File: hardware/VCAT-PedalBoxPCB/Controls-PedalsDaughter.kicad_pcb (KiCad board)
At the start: 2 copper layers, 53 x 66.2 mm, 105 parts, among them IC1 AP2205-W5-7, IC2 AP2205-W5-7, J3 Conn_02x03_Top_Bottom, J4 Conn_02x06_Top_Bottom, J5 Conn_02x04_Top_Bottom, U1 TLV9002QDRQ1, U2 INA241A5xD, U3 TLV9002QDRQ1, U4 INA241A5xD, U5 TLV9002QDRQ1

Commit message: mikea
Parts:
- R11, R12, R25, R26, R35, R36: value 100 -> 120

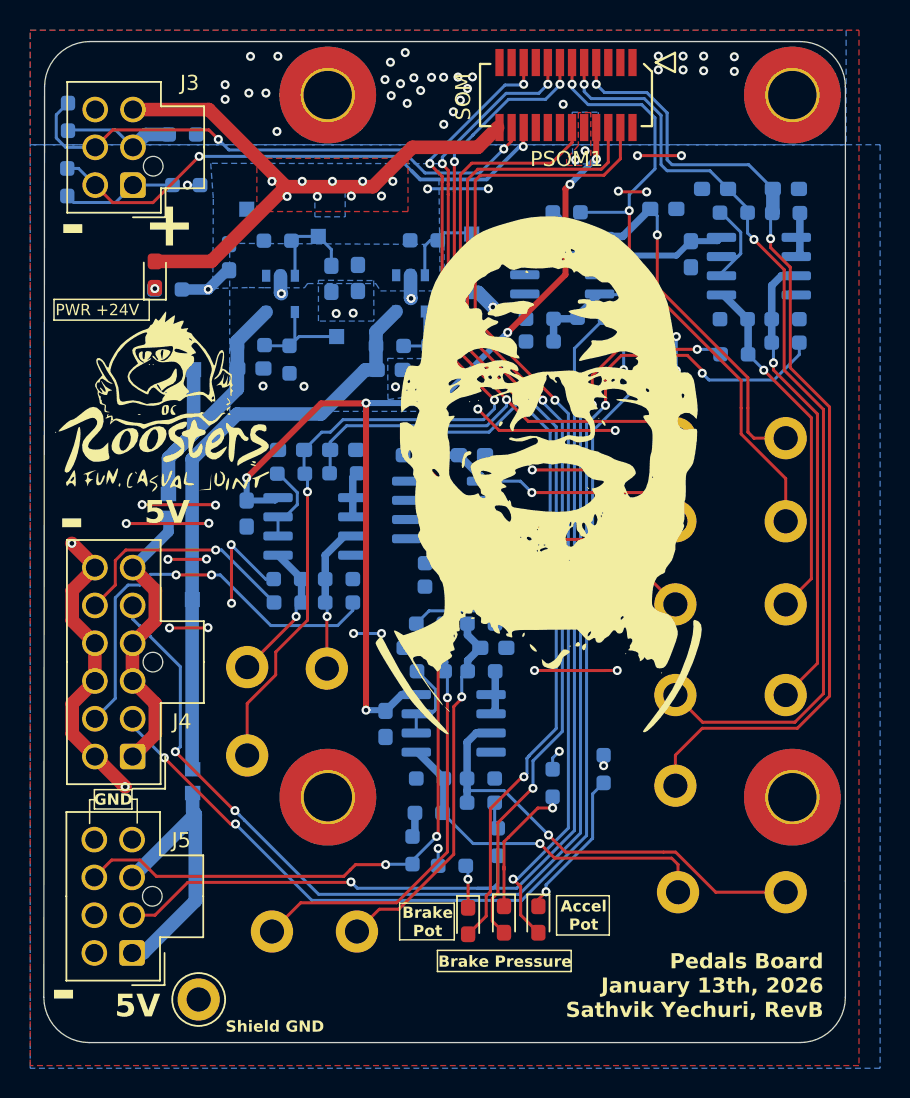
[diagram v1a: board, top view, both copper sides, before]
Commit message: layout fixes
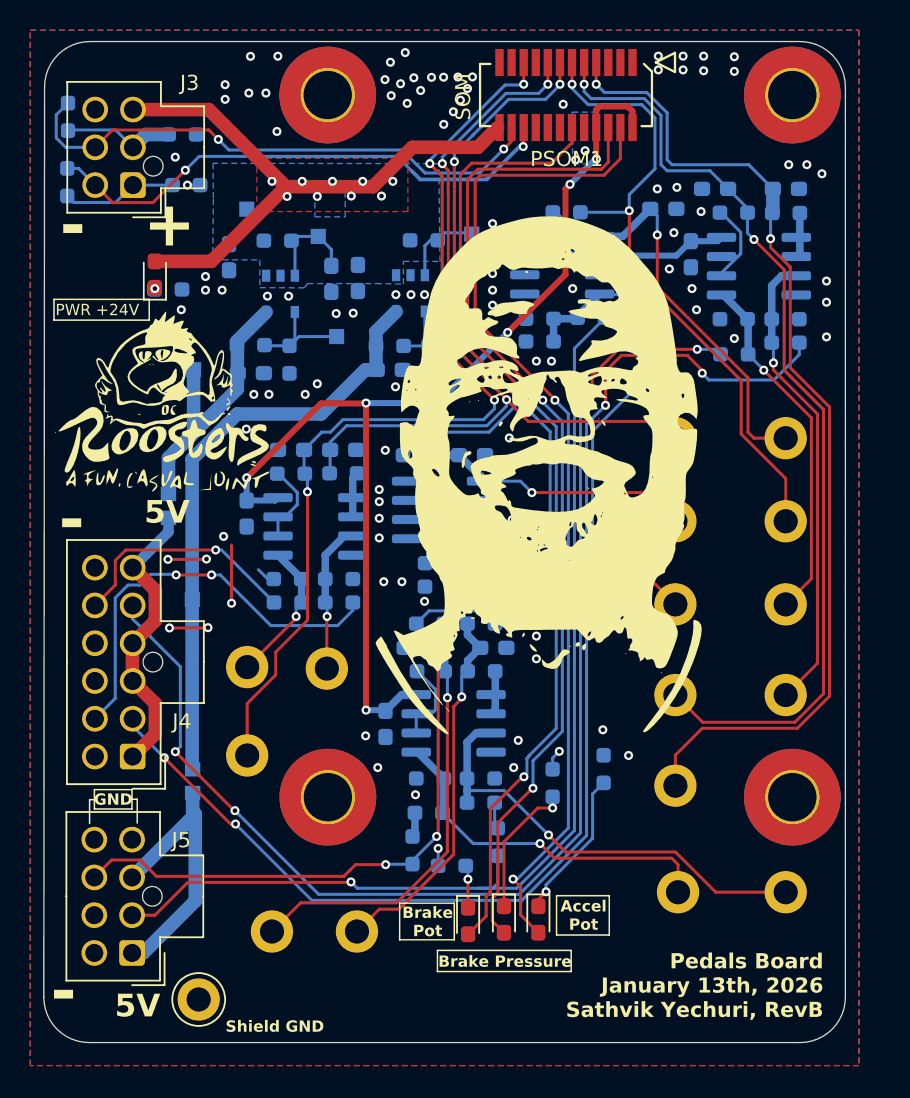
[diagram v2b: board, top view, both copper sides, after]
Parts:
- moved C7 0.32 mm to (134.6, 92.7)
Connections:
- C1 pad 1: +VDDA -> +3.3V
- C1 pad 2: GNDA -> GND
- C10 pad 2: GNDA -> GND
- C11 pad 1: GNDA -> GND
- C12 pad 1: GNDA -> GND
- C17 pad 1: +VDDA -> +3.3V
- C17 pad 2: GNDA -> GND
- C18 pad 1: GNDA -> GND
- C19 pad 1: GNDA -> GND
- C2 pad 1: GNDA -> GND
- C3 pad 1: GNDA -> GND
- C6 pad 1: +VDDA -> +3.3V
- C6 pad 2: GNDA -> GND
- C9 pad 2: GNDA -> GND
- J4 pad 10: GNDA -> GND
- J4 pad 12: GNDA -> GND
- J4 pad 7: GNDA -> GND
- J4 pad 9: GNDA -> GND
- J5 pad 5: GNDA -> GND
- J5 pad 6: GNDA -> GND
- PSOM1 pad 10: GNDA -> GND
- PSOM1 pad 2: unconnected-(PSOM1-+3.3v-Pad2) -> +3.3V
- PSOM1 pad 8: +VDDA -> +3.3V
- R1 pad 1: GNDA -> GND
- R16 pad 1: GNDA -> GND
- R23 pad 1: GNDA -> GND
- R24 pad 1: GNDA -> GND
- R30 pad 1: GNDA -> GND
- R31 pad 1: GNDA -> GND
- R32 pad 1: GNDA -> GND
- R4 pad 1: GNDA -> GND
- R40 pad 1: GNDA -> GND
- R5 pad 1: GNDA -> GND
- U1 pad 4: GNDA -> GND
- U1 pad 8: +VDDA -> +3.3V
- U2 pad 1: GNDA -> GND
- U2 pad 2: GNDA -> GND
- U2 pad 3: GNDA -> GND
- U2 pad 4: GNDA -> GND
- U2 pad 6: +VDDA -> +3.3V
- U2 pad 7: GNDA -> GND
- U3 pad 4: GNDA -> GND
- U3 pad 8: +VDDA -> +3.3V
- U4 pad 1: GNDA -> GND
- U4 pad 2: GNDA -> GND
- U4 pad 3: GNDA -> GND
- U4 pad 4: GNDA -> GND
- U4 pad 6: +VDDA -> +3.3V
- U4 pad 7: GNDA -> GND
- U5 pad 4: GNDA -> GND
- U5 pad 8: +VDDA -> +3.3V
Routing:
- net +3.3V: track 0.00 -> 90.3 mm, vias 0 -> 9
- net +VDDA: track 85.4 -> 0.00 mm, vias 9 -> 0
- net GNDA: track 80.5 -> 0.00 mm, vias 28 -> 0
- net GND: track 23.4 -> 13.8 mm, vias 54 -> 108
- removed copper zone on B.Cu, net GNDA
- removed copper zone on F.Cu, net GNDA

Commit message: lcsc + prod files
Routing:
- net /Pedals/Dual Op Amp Buffer Pots (main)/In2-: track 6.68 -> 7.31 mm
